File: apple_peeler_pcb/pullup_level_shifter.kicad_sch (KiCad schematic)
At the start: 4 parts, among them Q5 2N7002

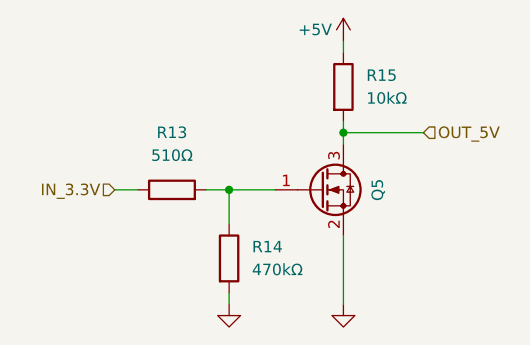
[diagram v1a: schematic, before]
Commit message: replace fancy debug connectors by pin header to save $8
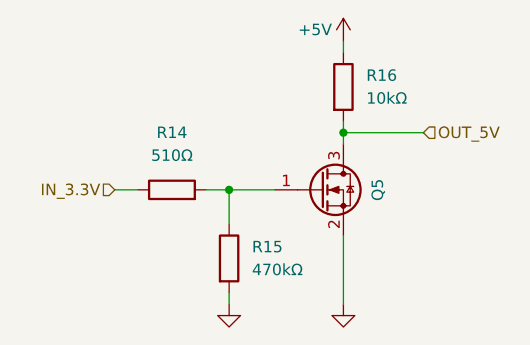
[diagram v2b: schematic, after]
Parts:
- renumbered R13 to R14, R14 to R15, R15 to R16
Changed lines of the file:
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@@
 		(dnp no)
 		(fields_autoplaced yes)
-		(property "Reference" "R13"
+		(property "Reference" "R14"
 			(at 129.54 88.9 90)
 			(effects
@@
 			(project "apple_peeler_pcb"
 				(path "/d5946b96-44a8-4a28-8641-19803e1510af/ab4760da-4146-4688-a275-418314974b55/566595e9-3b43-49bd-94a9-252623d78830"
-					(reference "R19")
+					(reference "R20")
 					(unit 1)
 				)
 				(path "/d5946b96-44a8-4a28-8641-19803e1510af/ab4760da-4146-4688-a275-418314974b55/745d0d17-7957-4c01-99cf-650fcabccc48"
-					(reference "R13")
+					(reference "R14")
 					(unit 1)
 				)
 				(path "/d5946b96-44a8-4a28-8641-19803e1510af/ab4760da-4146-4688-a275-418314974b55/873bc460-d915-4de5-a067-1951ea6c9d40"
-					(reference "R28")
+					(reference "R29")
 					(unit 1)
 				)
 				(path "/d5946b96-44a8-4a28-8641-19803e1510af/ab4760da-4146-4688-a275-418314974b55/b2b37924-8e56-4803-af0c-337a40ac95aa"
-					(reference "R16")
+					(reference "R17")
 					(unit 1)
 				)
 				(path "/d5946b96-44a8-4a28-8641-19803e1510af/ff7927ce-242d-46a3-8944-ca0e798b7163/bb525200-3afc-44a4-bfe6-0148de1ee95c"
-					(reference "R61")
+					(reference "R62")
 					(unit 1)
 				)
@@
 		(on_board yes)
 		(dnp no)
-		(property "Reference" "#PWR039"
+		(property "Reference" "#PWR038"
 			(at 148.59 114.3 0)
 			(effects
@@
 			(project "apple_peeler_pcb"
 				(path "/d5946b96-44a8-4a28-8641-19803e1510af/ab4760da-4146-4688-a275-418314974b55/566595e9-3b43-49bd-94a9-252623d78830"
-					(reference "#PWR045")
+					(reference "#PWR044")
 					(unit 1)
 				)
 				(path "/d5946b96-44a8-4a28-8641-19803e1510af/ab4760da-4146-4688-a275-418314974b55/745d0d17-7957-4c01-99cf-650fcabccc48"
-					(reference "#PWR039")
+					(reference "#PWR038")
 					(unit 1)
 				)
 				(path "/d5946b96-44a8-4a28-8641-19803e1510af/ab4760da-4146-4688-a275-418314974b55/873bc460-d915-4de5-a067-1951ea6c9d40"
-					(reference "#PWR054")
+					(reference "#PWR053")
 					(unit 1)
 				)
 				(path "/d5946b96-44a8-4a28-8641-19803e1510af/ab4760da-4146-4688-a275-418314974b55/b2b37924-8e56-4803-af0c-337a40ac95aa"
-					(reference "#PWR042")
+					(reference "#PWR041")
 					(unit 1)
 				)
 				(path "/d5946b96-44a8-4a28-8641-19803e1510af/ff7927ce-242d-46a3-8944-ca0e798b7163/bb525200-3afc-44a4-bfe6-0148de1ee95c"
-					(reference "#PWR0130")
+					(reference "#PWR0128")
 					(unit 1)
 				)
@@
 		(dnp no)
 		(fields_autoplaced yes)
-		(property "Reference" "R15"
+		(property "Reference" "R16"
 			(at 151.13 82.5499 0)
 			(effects
@@
 			(project "apple_peeler_pcb"
 				(path "/d5946b96-44a8-4a28-8641-19803e1510af/ab4760da-4146-4688-a275-418314974b55/566595e9-3b43-49bd-94a9-252623d78830"
-					(reference "R21")
+					(reference "R22")
 					(unit 1)
 				)
 				(path "/d5946b96-44a8-4a28-8641-19803e1510af/ab4760da-4146-4688-a275-418314974b55/745d0d17-7957-4c01-99cf-650fcabccc48"
-					(reference "R15")
+					(reference "R16")
 					(unit 1)
 				)
 				(path "/d5946b96-44a8-4a28-8641-19803e1510af/ab4760da-4146-4688-a275-418314974b55/873bc460-d915-4de5-a067-1951ea6c9d40"
-					(reference "R30")
+					(reference "R31")
 					(unit 1)
 				)
 				(path "/d5946b96-44a8-4a28-8641-19803e1510af/ab4760da-4146-4688-a275-418314974b55/b2b37924-8e56-4803-af0c-337a40ac95aa"
-					(reference "R18")
+					(reference "R19")
 					(unit 1)
 				)
 				(path "/d5946b96-44a8-4a28-8641-19803e1510af/ff7927ce-242d-46a3-8944-ca0e798b7163/bb525200-3afc-44a4-bfe6-0148de1ee95c"
-					(reference "R63")
+					(reference "R64")
 					(unit 1)
 				)
@@
 		(on_board yes)
 		(dnp no)
-		(property "Reference" "#PWR037"
+		(property "Reference" "#PWR036"
 			(at 135.89 114.3 0)
 			(effects
@@
 			(project "apple_peeler_pcb"
 				(path "/d5946b96-44a8-4a28-8641-19803e1510af/ab4760da-4146-4688-a275-418314974b55/566595e9-3b43-49bd-94a9-252623d78830"
-					(reference "#PWR043")
+					(reference "#PWR042")
 					(unit 1)
 				)
 				(path "/d5946b96-44a8-4a28-8641-19803e1510af/ab4760da-4146-4688-a275-418314974b55/745d0d17-7957-4c01-99cf-650fcabccc48"
-					(reference "#PWR037")
+					(reference "#PWR036")
 					(unit 1)
 				)
 				(path "/d5946b96-44a8-4a28-8641-19803e1510af/ab4760da-4146-4688-a275-418314974b55/873bc460-d915-4de5-a067-1951ea6c9d40"
-					(reference "#PWR052")
+					(reference "#PWR051")
 					(unit 1)
 				)
 				(path "/d5946b96-44a8-4a28-8641-19803e1510af/ab4760da-4146-4688-a275-418314974b55/b2b37924-8e56-4803-af0c-337a40ac95aa"
-					(reference "#PWR040")
+					(reference "#PWR039")
 					(unit 1)
 				)
 				(path "/d5946b96-44a8-4a28-8641-19803e1510af/ff7927ce-242d-46a3-8944-ca0e798b7163/bb525200-3afc-44a4-bfe6-0148de1ee95c"
-					(reference "#PWR0128")
+					(reference "#PWR0126")
 					(unit 1)
 				)
@@
 		(dnp no)
 		(fields_autoplaced yes)
-		(property "Reference" "R14"
+		(property "Reference" "R15"
 			(at 138.43 101.5999 0)
 			(effects
@@
 			(project "apple_peeler_pcb"
 				(path "/d5946b96-44a8-4a28-8641-19803e1510af/ab4760da-4146-4688-a275-418314974b55/566595e9-3b43-49bd-94a9-252623d78830"
-					(reference "R20")
+					(reference "R21")
 					(unit 1)
 				)
 				(path "/d5946b96-44a8-4a28-8641-19803e1510af/ab4760da-4146-4688-a275-418314974b55/745d0d17-7957-4c01-99cf-650fcabccc48"
-					(reference "R14")
+					(reference "R15")
 					(unit 1)
 				)
 				(path "/d5946b96-44a8-4a28-8641-19803e1510af/ab4760da-4146-4688-a275-418314974b55/873bc460-d915-4de5-a067-1951ea6c9d40"
-					(reference "R29")
+					(reference "R30")
 					(unit 1)
 				)
 				(path "/d5946b96-44a8-4a28-8641-19803e1510af/ab4760da-4146-4688-a275-418314974b55/b2b37924-8e56-4803-af0c-337a40ac95aa"
-					(reference "R17")
+					(reference "R18")
 					(unit 1)
 				)
 				(path "/d5946b96-44a8-4a28-8641-19803e1510af/ff7927ce-242d-46a3-8944-ca0e798b7163/bb525200-3afc-44a4-bfe6-0148de1ee95c"
-					(reference "R62")
+					(reference "R63")
 					(unit 1)
 				)
@@
 		(on_board yes)
 		(dnp no)
-		(property "Reference" "#PWR038"
+		(property "Reference" "#PWR037"
 			(at 148.59 82.55 0)
 			(effects
@@
 			(project "apple_peeler_pcb"
 				(path "/d5946b96-44a8-4a28-8641-19803e1510af/ab4760da-4146-4688-a275-418314974b55/566595e9-3b43-49bd-94a9-252623d78830"
-					(reference "#PWR044")
+					(reference "#PWR043")
 					(unit 1)
 				)
 				(path "/d5946b96-44a8-4a28-8641-19803e1510af/ab4760da-4146-4688-a275-418314974b55/745d0d17-7957-4c01-99cf-650fcabccc48"
-					(reference "#PWR038")
+					(reference "#PWR037")
 					(unit 1)
 				)
 				(path "/d5946b96-44a8-4a28-8641-19803e1510af/ab4760da-4146-4688-a275-418314974b55/873bc460-d915-4de5-a067-1951ea6c9d40"
-					(reference "#PWR053")
+					(reference "#PWR052")
 					(unit 1)
 				)
 				(path "/d5946b96-44a8-4a28-8641-19803e1510af/ab4760da-4146-4688-a275-418314974b55/b2b37924-8e56-4803-af0c-337a40ac95aa"
-					(reference "#PWR041")
+					(reference "#PWR040")
 					(unit 1)
 				)
 				(path "/d5946b96-44a8-4a28-8641-19803e1510af/ff7927ce-242d-46a3-8944-ca0e798b7163/bb525200-3afc-44a4-bfe6-0148de1ee95c"
-					(reference "#PWR0129")
-					(unit 1)
-				)
+					(reference "#PWR0127")
+					(unit 1)
+				)
